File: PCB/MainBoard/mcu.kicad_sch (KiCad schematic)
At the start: 1 part, among them U1 ESP32-S3-WROOM-1

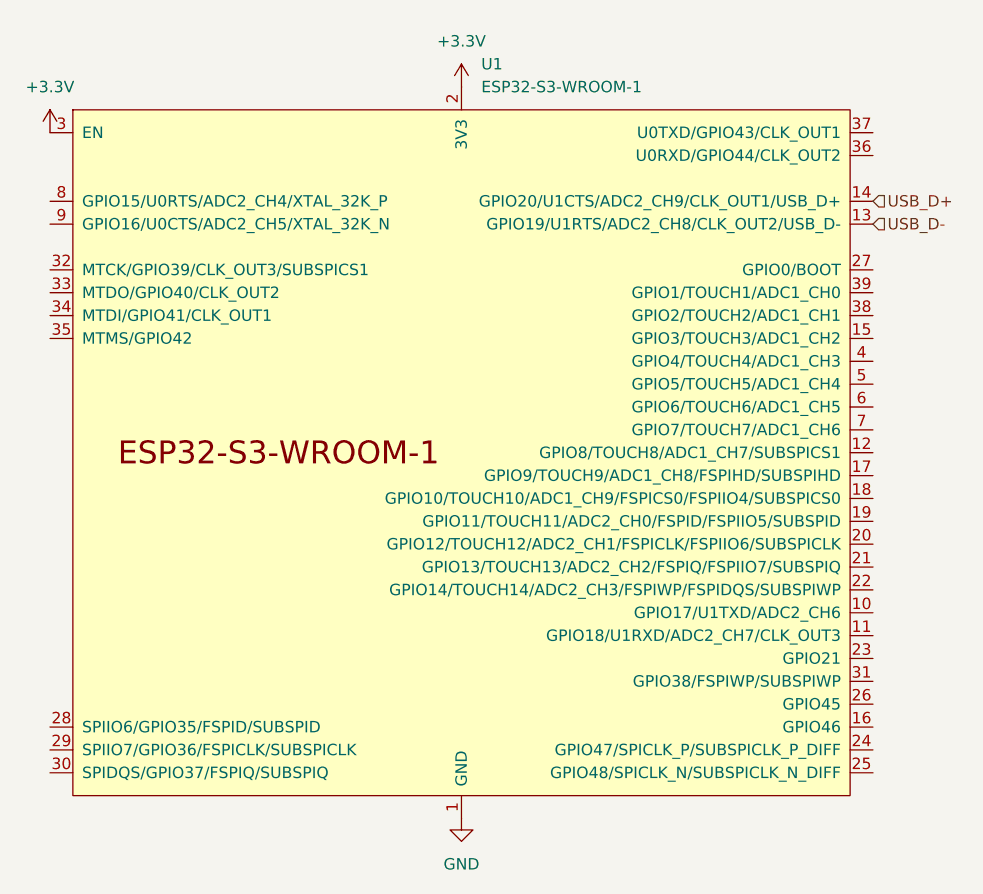
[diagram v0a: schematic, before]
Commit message: Repaired IMU and ESP symbols and footprints
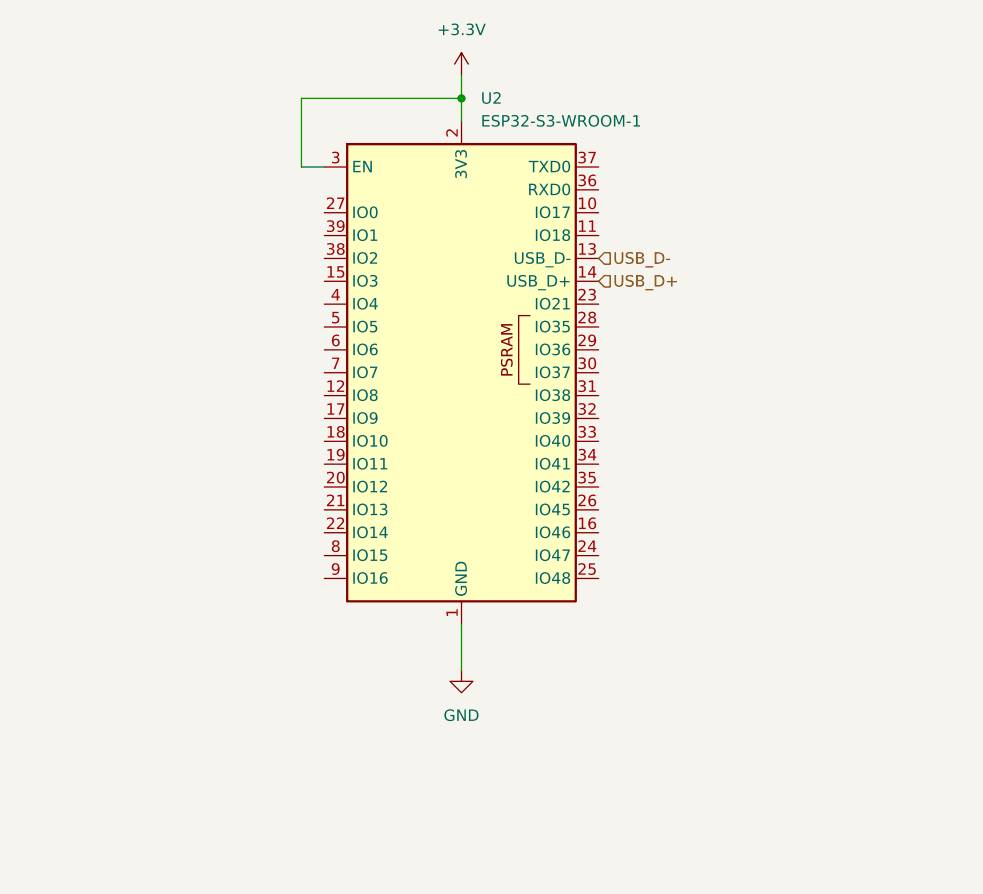
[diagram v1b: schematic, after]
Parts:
- removed U1: ESP32-S3-WROOM-1, PCM_Espressif:ESP32-S3-WROOM-1U, symbol PCM_Espressif:ESP32-S3-WROOM-1
- added U2: ESP32-S3-WROOM-1, RF_Module:ESP32-S3-WROOM-1U, symbol RF_Module:ESP32-S3-WROOM-1
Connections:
- net +3.3V: now also U2.2 (3V3), U2.3 (EN)
- net GND: now also U2.1 (GND), U2.40 (GND), U2.41 (GND)
- net USB_D+: now also U2.14 (USB_D+)
- net USB_D-: now also U2.13 (USB_D-)

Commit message: Added Buck converter
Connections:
- net INT2: now reaches U2.16 (IO46)
- net EN_LIDAR_MOT: now reaches U2.25 (IO48)
- net INT1: now reaches U2.26 (IO45)
- net SDA: now reaches U2.34 (IO41)
- net SCL: now reaches U2.35 (IO42)
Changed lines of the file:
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@@
+		)
+	)
+	(hierarchical_label "EN_LIDAR_MOT"
+		(shape output)
+		(at 105.41 95.25 0)
+		(effects
+			(font
+				(size 1.27 1.27)
+			)
+			(justify left)
+		)
+	)
+	(hierarchical_label "INT1"
+		(shape input)
+		(at 105.41 87.63 0)
+		(effects
+			(font
+				(size 1.27 1.27)
+			)
+			(justify left)
 		)
 	)
@@
 		(effects
 			(font
+				(size 1.27 1.27)
+			)
+			(justify left)
+		)
+	)
+	(hierarchical_label "SDA"
+		(shape output)
+		(at 105.41 82.55 0)
+		(effects
+			(font
+				(size 1.27 1.27)
+			)
+			(justify left)
+		)
+	)
+	(hierarchical_label "INT2"
+		(shape input)
+		(at 105.41 90.17 0)
+		(effects
+			(font
+				(size 1.27 1.27)
+			)
+			(justify left)
+		)
+	)
+	(hierarchical_label "SCL"
+		(shape output)
+		(at 105.41 85.09 0)
+		(effects
+			(font
